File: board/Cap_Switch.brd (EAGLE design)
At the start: 40 x 25.4 mm, 9 parts, among them K1 TOS TLP241A, Q1 PN2222ABU, Q2 PN2222ABU

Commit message: boards orderedd
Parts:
- moved R1 11.4 mm to (32.8, 16.1)
- moved R2 2.00 mm to (31.0, 5.08)
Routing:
- net Q1-DRIVE: track 37.6 -> 33.0 mm
- net TRIGGER: track 16.8 -> 20.7 mm
- net GND: track 53.0 -> 55.4 mm
- net Q2-DRIVE: track 34.7 -> 36.4 mm

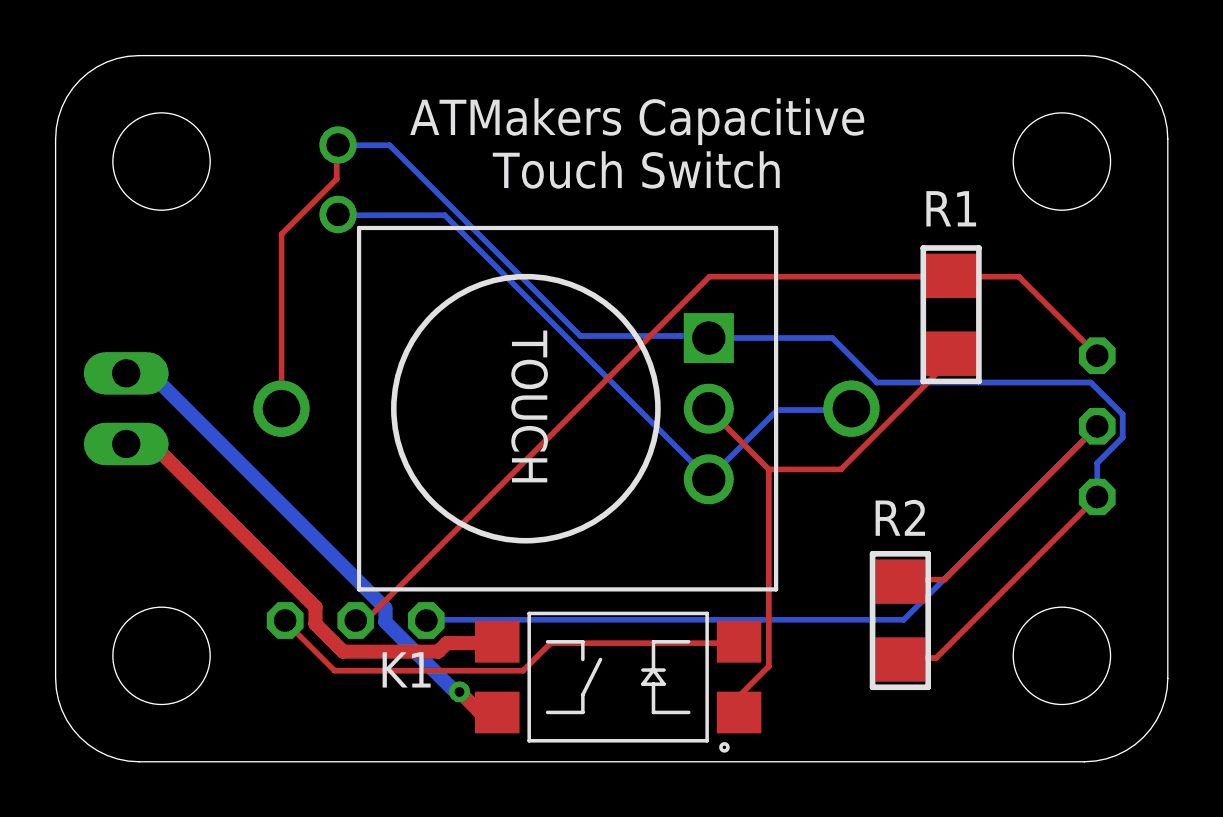
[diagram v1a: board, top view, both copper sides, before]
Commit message: fixed coin cell polarity, new PH con
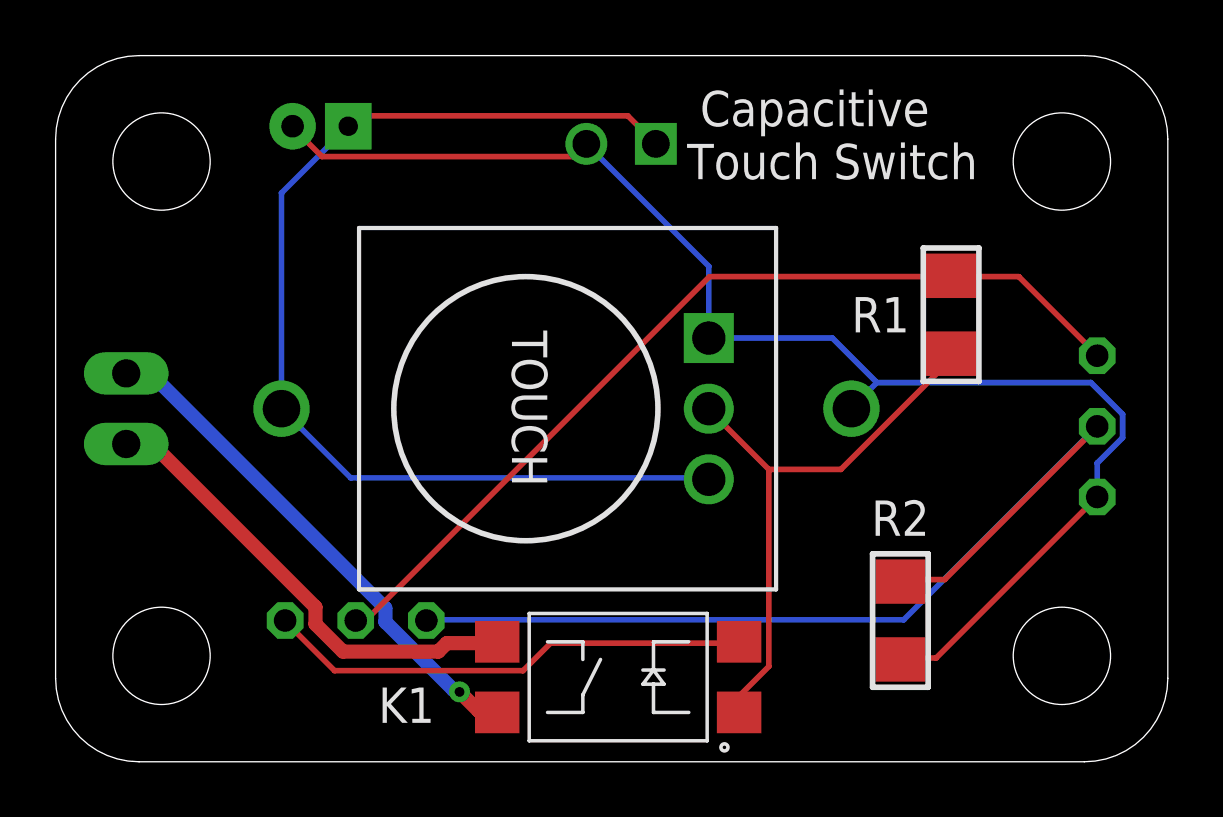
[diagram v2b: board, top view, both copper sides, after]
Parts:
- removed JS1: JST B2B-XH-A, Connector_writable:B2B-XH-A
- added B2.1: B2B-XH-2, Connector_writable:B2B-XH-A
- added B2.2: B2B-PH-2, jst-ph:JST-PH2
- B1: value KEYSTONE 1026 -> KEYSTONE 103; device home:1026_KEY -> home:1026_KEY-103
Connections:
- net GND: now also B1.-, B2.1.2, B2.2.2; no longer B1.+, JS1.2
- net V+: now also B1.+, B2.1.1, B2.2.1; no longer B1.-, JS1.1
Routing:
- net V+: track 23.5 -> 39.2 mm
- net GND: track 55.4 -> 50.2 mm
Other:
- board text added: "Capacitive"
- board text added: "Touch Switch"
- board text added: "rev 2b"
- board text removed: "ATMakers Capacitive Touch Switch"
